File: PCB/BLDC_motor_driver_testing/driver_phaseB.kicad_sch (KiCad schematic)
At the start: 22 parts, among them Q3 IRF540N, Q4 IRF540N, U5 IR2104, U6 INA240A2D, U7 LMV393

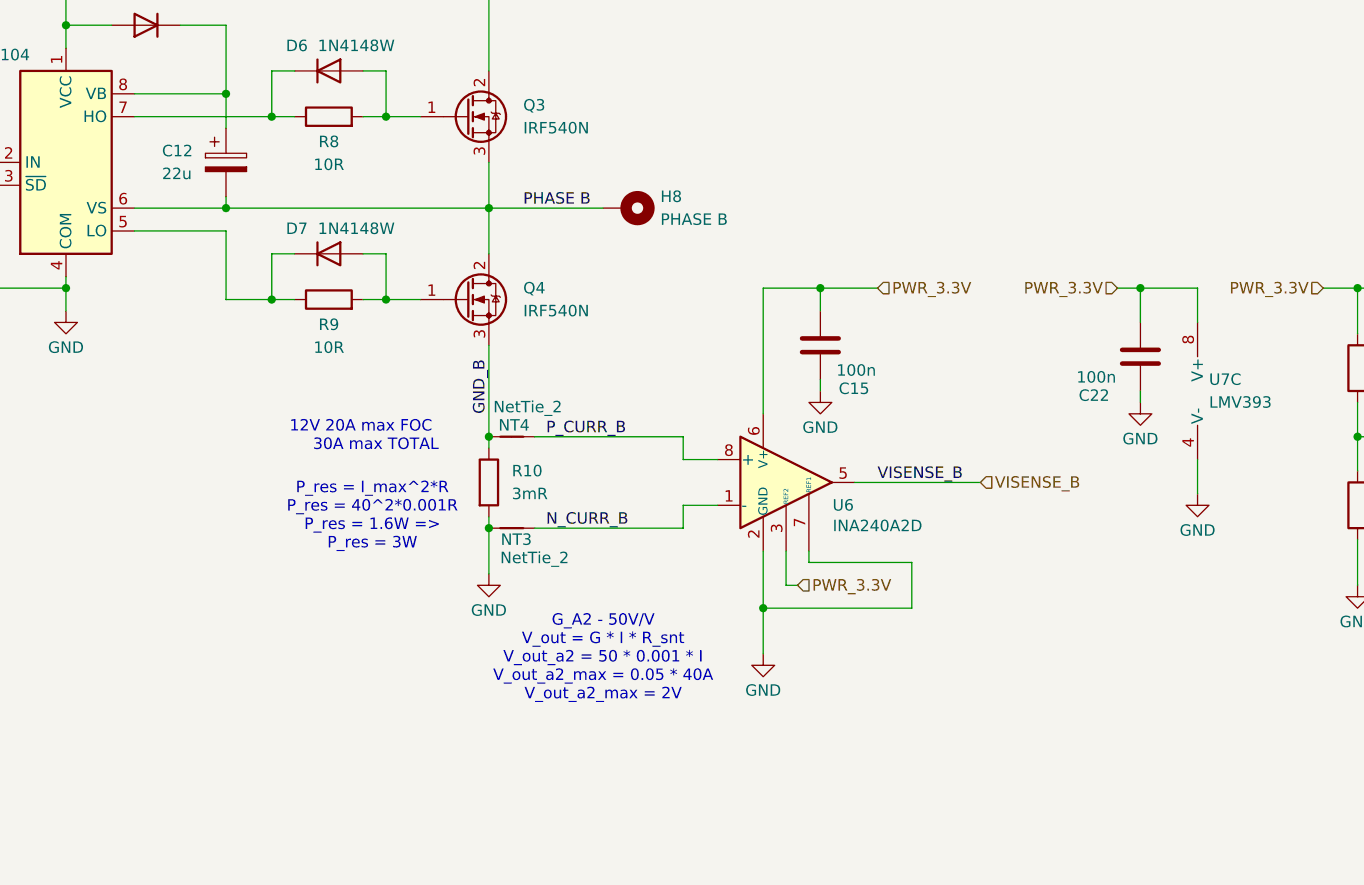
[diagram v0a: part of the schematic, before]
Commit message: selected bootstrap caps and shunt resistor and csa gain
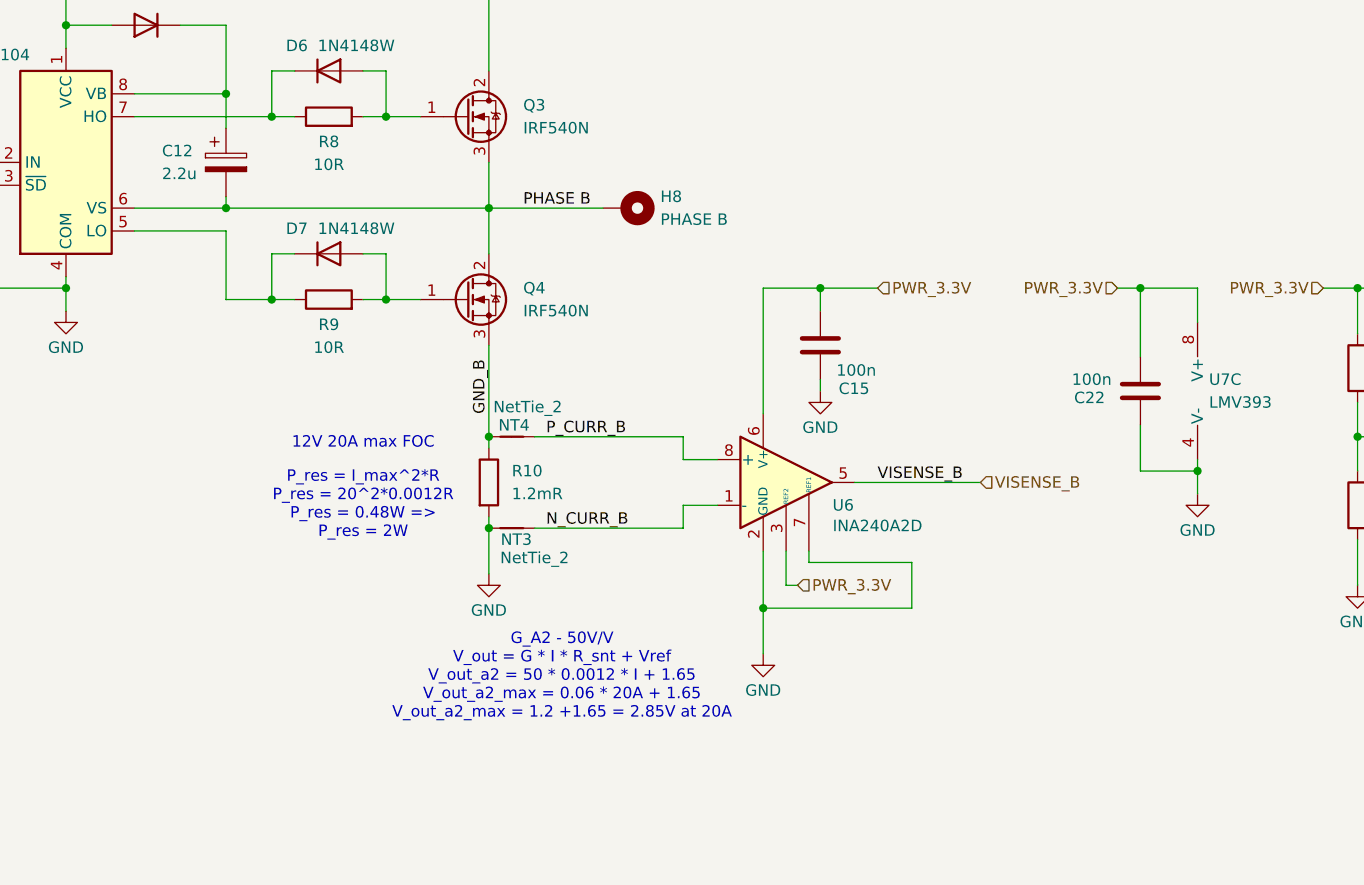
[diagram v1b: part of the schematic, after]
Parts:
- C12: value 22u -> 2.2u; footprint Capacitor_Tantalum_SMD:CP_EIA-3216-18_Kemet-A_HandSolder -> Capacitor_SMD:C_0805_2012Metric_Pad1.18x1.45mm_HandSolder
- R10: value 3mR -> 1.2mR
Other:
- note added: "12V 20A max FOC"
- note added: "G_A2 - 50V/V V_out = G * I * R_snt + Vref V_out_a2 = 50 * 0.0012 * I + 1.65 V_out_a2_max = 0.06 * 20A + 1.65 V_out_a2_max = 1.2 +1.65 = 2.85V at 20A"
- note added: "P_res = I_max^2*R P_res = 20^2*0.0012R P_res = 0.48W => P_res = 2W"
- note removed: "12V 20A max FOC 30A max TOTAL"
- note removed: "G_A2 - 50V/V V_out = G * I * R_snt V_out_a2 = 50 * 0.001 * I V_out_a2_max = 0.05 * 40A V_out_a2_max = 2V"
- note removed: "P_res = I_max^2*R P_res = 40^2*0.001R P_res = 1.6W => P_res = 3W"
- moved on the sheet: C22
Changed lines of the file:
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@@
 	(generator_version "9.0")
 	(paper "A4")
-	(text "12V 20A max FOC\n	  30A max TOTAL"
+	(text "12V 20A max FOC"
 		(exclude_from_sim no)
-		(at 98.806 110.49 0)
+		(at 99.06 111.252 0)
 		(effects
 			(font
@@
 		)
 	)
-	(text "G_A2 - 50V/V\nV_out = G * I * R_snt\nV_out_a2 = 50 * 0.001 * I\nV_out_a2_max = 0.05 * 40A\nV_out_a2_max = 2V"
+	(text "G_A2 - 50V/V\nV_out = G * I * R_snt + Vref\nV_out_a2 = 50 * 0.0012 * I + 1.65\nV_out_a2_max = 0.06 * 20A + 1.65\nV_out_a2_max = 1.2 +1.65 = 2.85V at 20A"
 		(exclude_from_sim no)
-		(at 125.73 135.128 0)
+		(at 121.158 137.16 0)
 		(effects
 			(font
@@
 		)
 	)
-	(text "P_res = I_max^2*R\nP_res = 40^2*0.001R\nP_res = 1.6W =>\nP_res = 3W"
+	(text "BLDC Driver Phase B"
 		(exclude_from_sim no)
-		(at 100.076 119.38 0)
+		(at 197.358 189.738 0)
 		(effects
 			(font
@@
 		)
 	)
-	(text "BLDC Driver Phase B"
+	(text "P_res = I_max^2*R\nP_res = 20^2*0.0012R\nP_res = 0.48W =>\nP_res = 2W"
 		(exclude_from_sim no)
-		(at 197.358 189.738 0)
+		(at 99.06 118.11 0)
 		(effects
 			(font
@@
 	)
 	(junction
+		(at 191.77 114.3)
+		(diameter 0)
+		(color 0 0 0 0)
+	)
+	(junction
 		(at 209.55 110.49)
 		(diameter 0)
@@
 	(wire
 		(pts
-			(xy 185.42 97.79) (xy 185.42 93.98)
+			(xy 185.42 101.6) (xy 185.42 93.98)
 		)
 		(stroke
@@
 	(wire
 		(pts
-			(xy 191.77 116.84) (xy 191.77 113.03)
-		)
-		(stroke
-			(width 0)
-			(type default)
-		)
-	)
-	(wire
-		(pts
 			(xy 66.04 92.71) (xy 66.04 93.98)
 		)
@@
 	(wire
 		(pts
-			(xy 185.42 105.41) (xy 185.42 106.68)
+			(xy 185.42 109.22) (xy 185.42 114.3)
 		)
 		(stroke
@@
 	(wire
 		(pts
+			(xy 191.77 114.3) (xy 191.77 113.03)
+		)
+		(stroke
+			(width 0)
+			(type default)
+		)
+	)
+	(wire
+		(pts
 			(xy 209.55 110.49) (xy 209.55 114.3)
 		)
@@
 	(wire
 		(pts
+			(xy 191.77 114.3) (xy 191.77 116.84)
+		)
+		(stroke
+			(width 0)
+			(type default)
+		)
+	)
+	(wire
+		(pts
 			(xy 101.6 90.17) (xy 101.6 95.25)
 		)
@@
 	(wire
 		(pts
+			(xy 185.42 114.3) (xy 191.77 114.3)
+		)
+		(stroke
+			(width 0)
+			(type default)
+		)
+	)
+	(wire
+		(pts
 			(xy 101.6 74.93) (xy 105.41 74.93)
 		)
@@
 	(symbol
 		(lib_id "Device:C")
-		(at 185.42 101.6 0)
+		(at 185.42 105.41 0)
 		(unit 1)
 		(exclude_from_sim no)
@@
 		(dnp no)
 		(property "Reference" "C22"
-			(at 178.562 105.918 0)
+			(at 178.054 106.172 0)
 			(effects
 				(font
@@
 		)
 		(property "Value" "100n"
-			(at 178.308 103.886 0)
+			(at 177.8 104.14 0)
 			(effects
 				(font
@@
 		)
 		(property "Footprint" "Capacitor_SMD:C_0805_2012Metric_Pad1.18x1.45mm_HandSolder"
-			(at 186.3852 105.41 0)
+			(at 186.3852 109.22 0)
 			(effects
 				(font
@@
 		)
 		(property "Datasheet" "~"
-			(at 185.42 101.6 0)
+			(at 185.42 105.41 0)
 			(effects
 				(font
@@
 		)
 		(property "Description" "Unpolarized capacitor"
-			(at 185.42 101.6 0)
+			(at 185.42 105.41 0)
 			(effects
 				(font
@@
 			)
 		)
-		(property "Value" "22u"
+		(property "Value" "2.2u"
 			(at 76.708 81.28 0)
 			(effects
@@
 			)
 		)
-		(property "Footprint" "Capacitor_Tantalum_SMD:CP_EIA-3216-18_Kemet-A_HandSolder"
+		(property "Footprint" "Capacitor_SMD:C_0805_2012Metric_Pad1.18x1.45mm_HandSolder"
 			(at 84.7852 83.82 0)
 			(effects
@@
 			)
 		)
-		(property "Value" "3mR"
+		(property "Value" "1.2mR"
 			(at 115.57 116.8399 0)
 			(effects
@@
 					(unit 1)
 				)
-			)
-		)
-	)
-	(symbol
-		(lib_id "power:GND")
-		(at 185.42 106.68 0)
-		(unit 1)
-		(exclude_from_sim no)
-		(in_bom yes)
-		(on_board yes)
-		(dnp no)
-		(property "Reference" "#PWR040"
-			(at 185.42 113.03 0)
-			(effects
-				(font
-					(size 1.27 1.27)
-				)
-				(hide yes)
-			)
-		)
-		(property "Value" "GND"
-			(at 185.42 110.744 0)
-			(effects
-				(font
-					(size 1.27 1.27)
-				)
-			)
-		)
-		(property "Footprint" ""
-			(at 185.42 106.68 0)
-			(effects
-				(font
-					(size 1.27 1.27)
-				)
-				(hide yes)
-			)
-		)
-		(property "Datasheet" ""
-			(at 185.42 106.68 0)
-			(effects
-				(font
-					(size 1.27 1.27)
-				)
-				(hide yes)
-			)
-		)
-		(property "Description" "Power symbol creates a global label with name \"GND\" , ground"
-			(at 185.42 106.68 0)
-			(effects
-				(font
-					(size 1.27 1.27)
-				)
-				(hide yes)
-			)
-		)
-		(pin "1"
-		)
-		(instances
-			(project "BLDC_motor_driver_testing"
-				(path "/4ecc7e27-f6b5-41f4-b6cd-6ae03975803c/75eb2a18-d734-4bd7-a689-095bb5279c38"
-					(reference "#PWR040")
-					(unit 1)
-				)

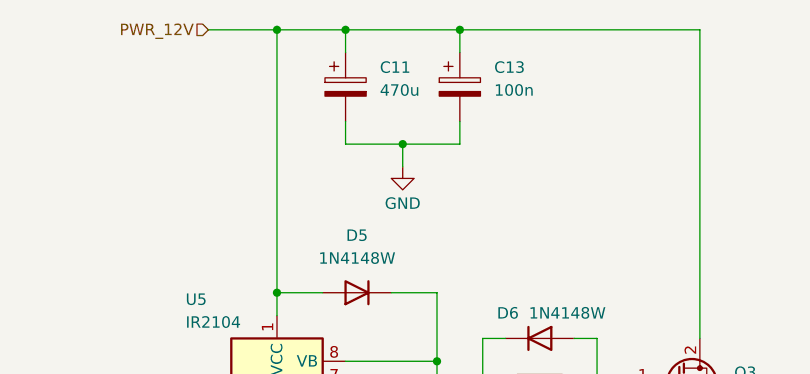
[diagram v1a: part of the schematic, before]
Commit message: Final version of BLDC test driver
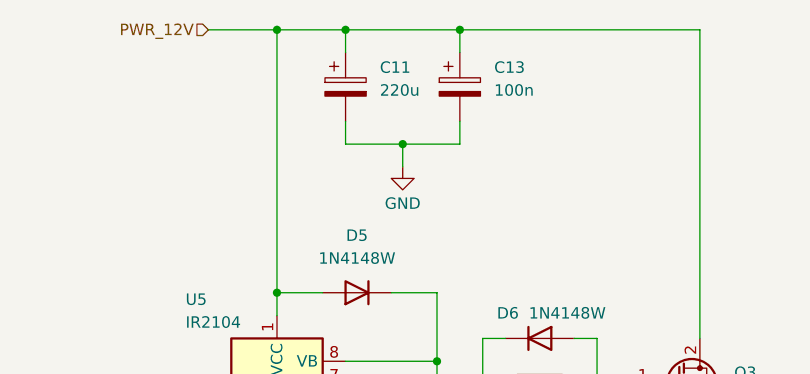
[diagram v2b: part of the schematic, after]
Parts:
- C11: value 470u -> 220u; JLCPCB Part # (none) -> C3340
- C12: JLCPCB Part # (none) -> C342739
- C13: JLCPCB Part # (none) -> C2976899
- R10: JLCPCB Part # (none) -> C51934143
- U6: JLCPCB Part # (none) -> C2060768
- U7: footprint Package_SO:VSSOP-8_2.3x2mm_P0.5mm -> Package_SO:VSSOP-8_3x3mm_P0.65mm; JLCPCB Part # (none) -> C352866
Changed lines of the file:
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@@
+			)
+		)
+		(property "JLCPCB Part #" "C2976899"
+			(at 86.36 41.91 0)
+			(effects
+				(font
+					(size 1.27 1.27)
+				)
+				(hide yes)
 			)
 		)
@@
 			)
 		)
-		(property "Footprint" "Package_SO:VSSOP-8_2.3x2mm_P0.5mm"
+		(property "Footprint" "Package_SO:VSSOP-8_3x3mm_P0.65mm"
 			(at 240.03 124.46 0)
 			(effects
@@
 		)
 		(property "Description" "Dual General-Purpose Low-Voltage Comparator, SOIC-8/TSSOP-8/VSSOP-8"
+			(at 240.03 124.46 0)
+			(effects
+				(font
+					(size 1.27 1.27)
+				)
+				(hide yes)
+			)
+		)
+		(property "JLCPCB Part #" "C352866"
 			(at 240.03 124.46 0)
 			(effects
@@
 			)
 		)
-		(property "Value" "470u"
+		(property "Value" "220u"
 			(at 77.47 42.2909 0)
 			(effects
@@
 			)
 		)
+		(property "JLCPCB Part #" "C3340"
+			(at 73.66 41.91 0)
+			(effects
+				(font
+					(size 1.27 1.27)
+				)
+				(hide yes)
+			)
+		)
 		(pin "1"
 		)
@@
 			)
 		)
+		(property "JLCPCB Part #" "C2060768"
+			(at 146.05 115.57 0)
+			(effects
+				(font
+					(size 1.27 1.27)
+				)
+				(hide yes)
+			)
+		)
 		(pin "2"
 		)
@@
 		)
 		(property "Description" "Polarized capacitor"
+			(at 83.82 80.01 0)
+			(effects
+				(font
+					(size 1.27 1.27)
+				)
+				(hide yes)
+			)
+		)
+		(property "JLCPCB Part #" "C342739"
 			(at 83.82 80.01 0)
 			(effects
@@
 			)
 		)
+		(property "JLCPCB Part #" "C51934143"
+			(at 113.03 115.57 0)
+			(effects
+				(font
+					(size 1.27 1.27)
+				)
+				(hide yes)
+			)
+		)
 		(pin "1"
 		)
@@
 			)
 		)
-		(property "Footprint" "Package_SO:VSSOP-8_2.3x2mm_P0.5mm"
+		(property "Footprint" "Package_SO:VSSOP-8_3x3mm_P0.65mm"
 			(at 194.31 105.41 0)
 			(effects
@@
 		)
 		(property "Description" "Dual General-Purpose Low-Voltage Comparator, SOIC-8/TSSOP-8/VSSOP-8"
+			(at 194.31 105.41 0)
+			(effects
+				(font
+					(size 1.27 1.27)
+				)
+				(hide yes)
+			)
+		)
+		(property "JLCPCB Part #" "C352866"
 			(at 194.31 105.41 0)
 			(effects
@@
 			)
 		)
-		(property "Footprint" "Package_SO:VSSOP-8_2.3x2mm_P0.5mm"
+		(property "Footprint" "Package_SO:VSSOP-8_3x3mm_P0.65mm"
 			(at 240.03 107.95 0)
 			(effects
@@
 			(at 240.03 107.95 0)
 			(effects
+				(font
+					(size 1.27 1.27)
+				)
+				(hide yes)
+			)
+		)
+		(property "JLCPCB Part #" "C352866"
+			(at 240.03 107.95 0)
+			(effects
